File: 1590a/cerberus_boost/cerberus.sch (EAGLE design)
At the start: 30 parts, among them Q1 2N5088, Q2 2N5088, Q3 2N5087

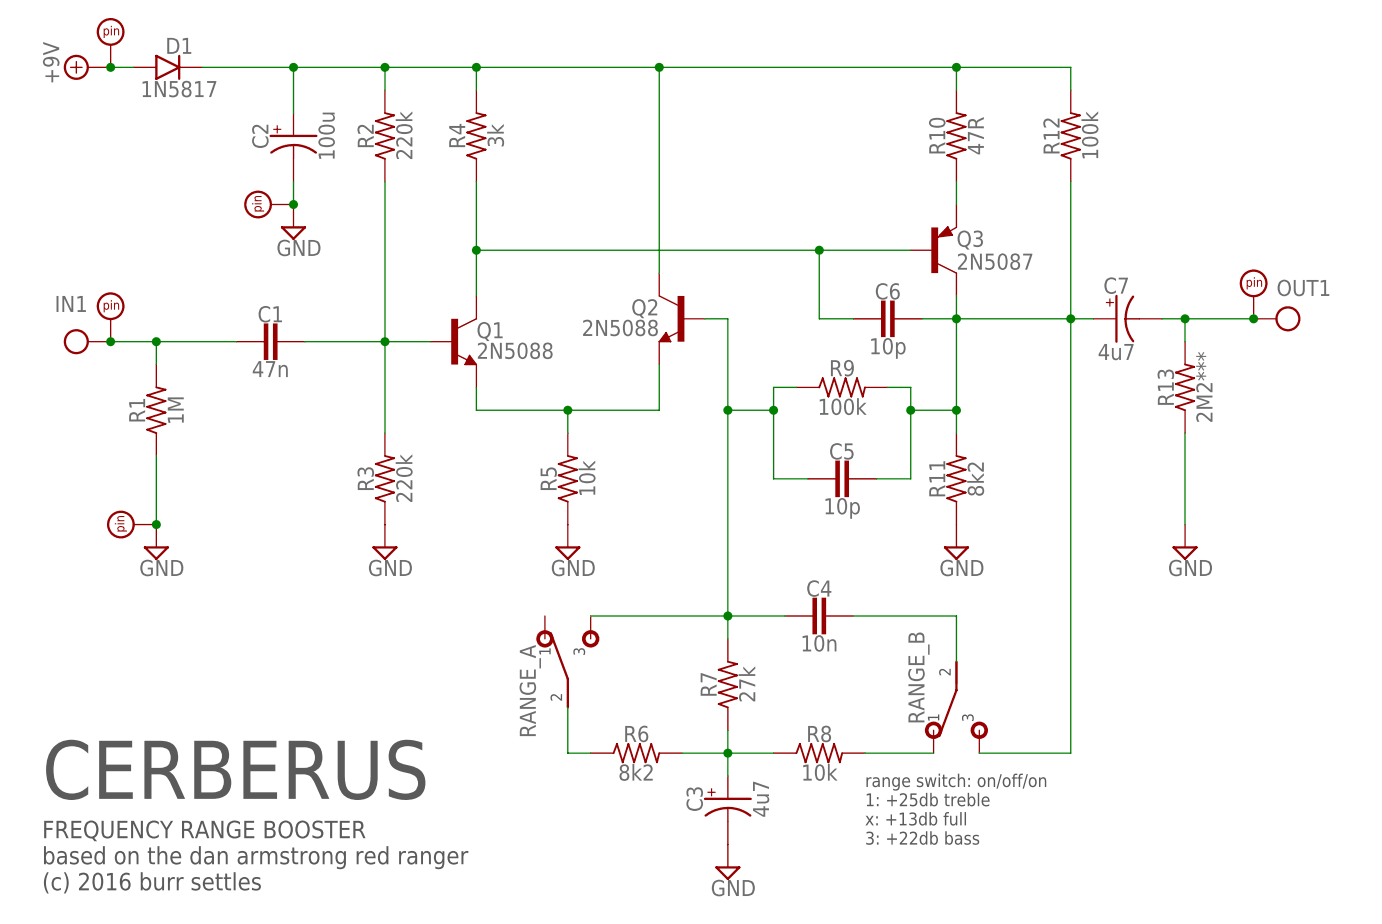
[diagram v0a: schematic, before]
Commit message: prettified schematics a bit
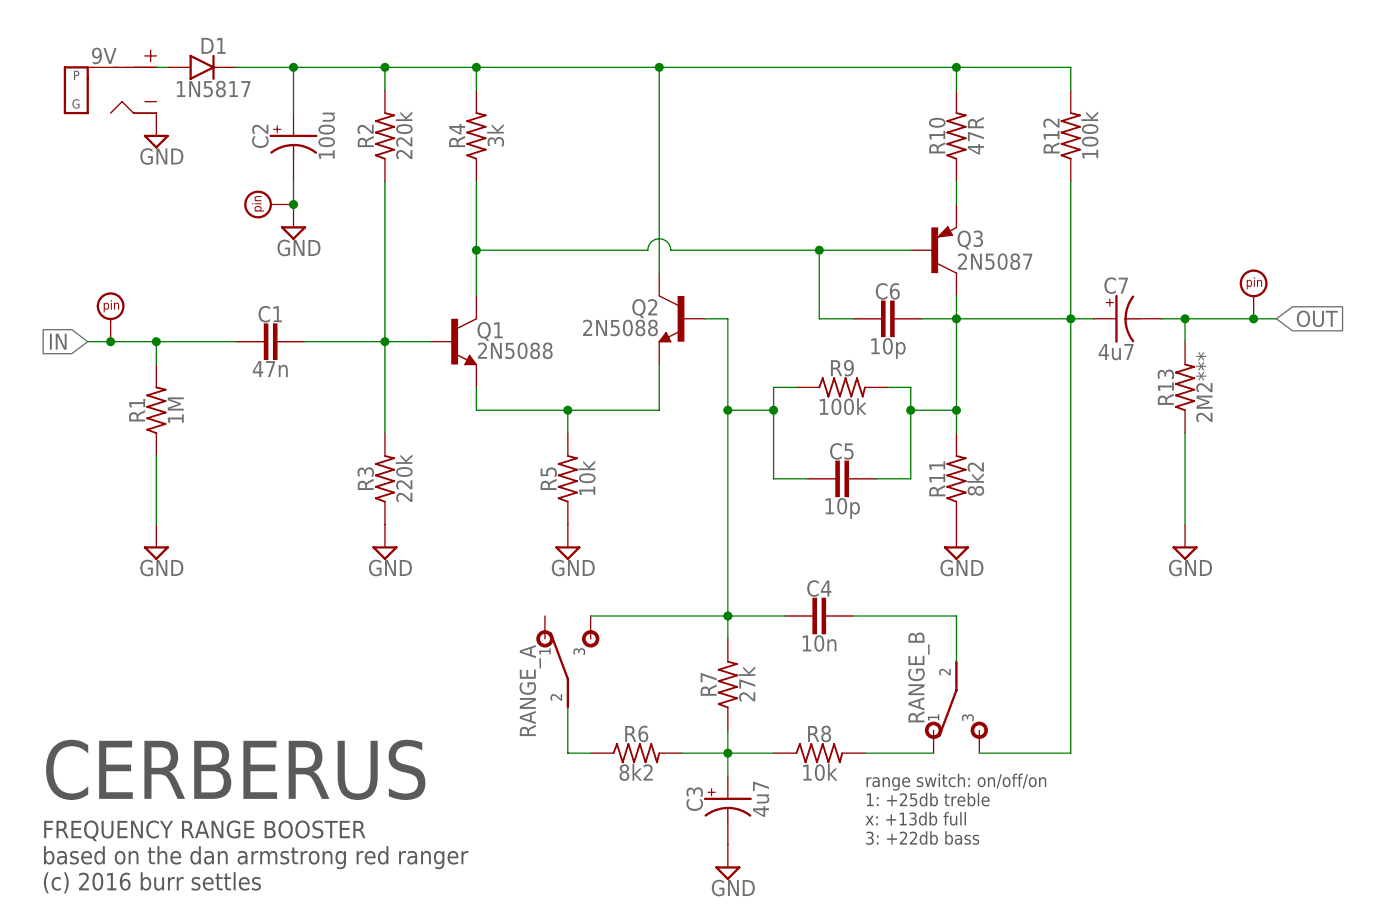
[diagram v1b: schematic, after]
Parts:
- removed PAD1: PADSQR, supply pins:PADSQR
- removed PAD3: PADRND, supply pins:PADRND
- added 9V: DC_MONO, jacks:DC_MONO
- D1: device diodes:DO41.2 -> diodes:DO41.3
- renumbered PAD2 to IN, PAD4 to GND, PAD5 to OUT
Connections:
- removed net +9V: D1.A, PAD1.P$1
- new net N$3: 9V.TIP, D1.A
- net GND: now also 9V.SLEEVE; no longer PAD3.P$1
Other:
- moved on the sheet: D1
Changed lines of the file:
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@@
 <drawing>
 <settings>
-<setting alwaysvectorfont="no"/>
+<setting alwaysvectorfont="yes"/>
 <setting verticaltext="up"/>
 </settings>
-<grid distance="0.1" unitdist="inch" unit="inch" style="lines" multiple="1" display="no" altdistance="0.01" altunitdist="inch" altunit="inch"/>
+<grid distance="0.05" unitdist="inch" unit="inch" style="lines" multiple="2" display="no" altdistance="0.01" altunitdist="inch" altunit="inch"/>
 <layers>
 <layer number="1" name="Top" color="4" fill="1" visible="no" active="no"/>
@@
 </classes>
 <parts>
-<part name="V1" library="gm-supply" deviceset="+9V" device=""/>
-<part name="IN1" library="gm-supply" deviceset="IN" device=""/>
-<part name="OUT1" library="gm-supply" deviceset="OUT" device=""/>
 <part name="C2" library="capacitors-elec" deviceset="050" device="1" value="100u"/>
 <part name="R2" library="resistors" deviceset="R_" device=".3B" value="220k"/>
@@
 <part name="GND5" library="gm-supply" deviceset="GND" device=""/>
 <part name="GND3" library="gm-supply" deviceset="GND" device=""/>
-<part name="PAD5" library="supply pins" deviceset="PAD" device="SQR"/>
-<part name="PAD2" library="supply pins" deviceset="PAD" device="SQR"/>
-<part name="PAD1" library="supply pins" deviceset="PAD" device="SQR"/>
-<part name="PAD3" library="supply pins" deviceset="PAD" device="RND"/>
-<part name="PAD4" library="supply pins" deviceset="PAD" device="RND"/>
+<part name="OUT" library="supply pins" deviceset="PAD" device="SQR"/>
+<part name="IN" library="supply pins" deviceset="PAD" device="SQR"/>
+<part name="GND" library="supply pins" deviceset="PAD" device="RND"/>
 <part name="R1" library="resistors" deviceset="R_" device=".3B" value="1M"/>
 <part name="GND1" library="gm-supply" deviceset="GND" device=""/>
@@
 <part name="R13" library="resistors" deviceset="R_" device=".3B" value="2M2***"/>
 <part name="GND7" library="gm-supply" deviceset="GND" device=""/>
-<part name="D1" library="diodes" deviceset="DO41" device=".2" value="1N5817"/>
+<part name="D1" library="diodes" deviceset="DO41" device=".3" value="1N5817"/>
+<part name="9V" library="jacks" deviceset="DC_MONO" device=""/>
+<part name="GND8" library="gm-supply" deviceset="GND" device=""/>
 </parts>
 <sheets>
@@
 </plain>
 <instances>
-<instance part="V1" gate="+9V" x="7.62" y="93.98" rot="R90"/>
-<instance part="IN1" gate="G$1" x="7.62" y="63.5"/>
-<instance part="OUT1" gate="G$1" x="139.7" y="66.04"/>
 <instance part="C2" gate="1" x="30.48" y="86.36" rot="MR270"/>
 <instance part="R2" gate="G$1" x="40.64" y="86.36" rot="R90"/>
@@
 <instance part="GND5" gate="GND" x="78.74" y="5.08"/>
 <instance part="GND3" gate="GND" x="40.64" y="40.64"/>
-<instance part="PAD5" gate="G$1" x="137.16" y="66.04"/>
-<instance part="PAD2" gate="G$1" x="10.16" y="63.5"/>
-<instance part="PAD1" gate="G$1" x="10.16" y="93.98"/>
-<instance part="PAD3" gate="G$1" x="15.24" y="43.18" rot="R90"/>
-<instance part="PAD4" gate="G$1" x="30.48" y="78.74" rot="R90"/>
+<instance part="OUT" gate="G$1" x="137.16" y="66.04"/>
+<instance part="IN" gate="G$1" x="10.16" y="63.5"/>
+<instance part="GND" gate="G$1" x="30.48" y="78.74" rot="R90"/>
 <instance part="R1" gate="G$1" x="15.24" y="55.88" rot="R90"/>
 <instance part="GND1" gate="GND" x="15.24" y="40.64"/>
@@
 <instance part="R13" gate="G$1" x="129.54" y="58.42" rot="R90"/>
 <instance part="GND7" gate="GND" x="129.54" y="40.64"/>
-<instance part="D1" gate="G$1" x="17.78" y="93.98"/>
+<instance part="D1" gate="G$1" x="21.59" y="93.98"/>
+<instance part="9V" gate="DC" x="10.16" y="91.44"/>
+<instance part="GND8" gate="GND" x="15.24" y="86.36"/>
 </instances>
 <busses>
 </busses>
 <nets>
-<net name="IN" class="0">
-<segment>
-<pinref part="IN1" gate="G$1" pin="IN"/>
-<pinref part="C1" gate="G$1" pin="2"/>
-<pinref part="PAD2" gate="G$1" pin="P$1"/>
-<wire x1="10.16" y1="63.5" x2="15.24" y2="63.5" width="0.1524" layer="91"/>
-<junction x="10.16" y="63.5"/>
-<pinref part="R1" gate="G$1" pin="2"/>
-<wire x1="15.24" y1="63.5" x2="24.13" y2="63.5" width="0.1524" layer="91"/>
-<wire x1="15.24" y1="60.96" x2="15.24" y2="63.5" width="0.1524" layer="91"/>
-<junction x="15.24" y="63.5"/>
-</segment>
-</net>
 <net name="N$1" class="0">
 <segment>
@@
 </segment>
 </net>
-<net name="+9V" class="0">
-<segment>
-<pinref part="D1" gate="G$1" pin="A"/>
-<wire x1="10.16" y1="93.98" x2="12.7" y2="93.98" width="0.1524" layer="91"/>
-<pinref part="PAD1" gate="G$1" pin="P$1"/>
-<junction x="10.16" y="93.98"/>
-<pinref part="V1" gate="+9V" pin="+9V"/>
-</segment>
-</net>
 <net name="N$2" class="0">
 <segment>
@@
 <wire x1="99.06" y1="73.66" x2="88.9" y2="73.66" width="0.1524" layer="91"/>
 <junction x="50.8" y="73.66"/>
-<wire x1="88.9" y1="73.66" x2="50.8" y2="73.66" width="0.1524" layer="91"/>
+<wire x1="88.9" y1="73.66" x2="72.39" y2="73.66" width="0.1524" layer="91"/>
+<wire x1="69.85" y1="73.66" x2="50.8" y2="73.66" width="0.1524" layer="91"/>
 <wire x1="92.71" y1="66.04" x2="88.9" y2="66.04" width="0.1524" layer="91"/>
 <wire x1="88.9" y1="66.04" x2="88.9" y2="73.66" width="0.1524" layer="91"/>
 <junction x="88.9" y="73.66"/>
 <pinref part="C6" gate="G$1" pin="2"/>
+<wire x1="69.85" y1="73.66" x2="72.39" y2="73.66" width="0.1524" layer="91" curve="-180" cap="flat"/>
 </segment>
 </net>
@@
 </segment>
 </net>
-<net name="OUT" class="0">
-<segment>
-<pinref part="OUT1" gate="G$1" pin="OUT"/>
-<pinref part="PAD5" gate="G$1" pin="P$1"/>
-<pinref part="C7" gate="1" pin="-"/>
-<wire x1="127" y1="66.04" x2="129.54" y2="66.04" width="0.1524" layer="91"/>
-<wire x1="129.54" y1="66.04" x2="137.16" y2="66.04" width="0.1524" layer="91"/>
-<pinref part="R13" gate="G$1" pin="2"/>
-<wire x1="129.54" y1="63.5" x2="129.54" y2="66.04" width="0.1524" layer="91"/>
-<junction x="129.54" y="66.04"/>
-<junction x="137.16" y="66.04"/>
-</segment>
-</net>
 <net name="N$10" class="0">
 <segment>
@@
 <pinref part="C2" gate="1" pin="-"/>
 <pinref part="GND2" gate="GND" pin="GND"/>
-<pinref part="PAD4" gate="G$1" pin="P$1"/>
+<pinref part="GND" gate="G$1" pin="P$1"/>
 <junction x="30.48" y="78.74"/>
 <wire x1="30.48" y1="78.74" x2="30.48" y2="81.28" width="0.1524" layer="91"/>
@@
 <wire x1="15.24" y1="50.8" x2="15.24" y2="43.18" width="0.1524" layer="91"/>
 <pinref part="GND1" gate="GND" pin="GND"/>
-<pinref part="PAD3" gate="G$1" pin="P$1"/>
-<junction x="15.24" y="43.18"/>
 </segment>
 <segment>
@@
 <wire x1="129.54" y1="53.34" x2="129.54" y2="43.18" width="0.1524" layer="91"/>
 </segment>
+<segment>
+<pinref part="9V" gate="DC" pin="SLEEVE"/>
+<pinref part="GND8" gate="GND" pin="GND"/>
+</segment>
 </net>
 <net name="N$7" class="0">
 <segment>
 <pinref part="R12" gate="G$1" pin="2"/>
-<wire x1="20.32" y1="93.98" x2="30.48" y2="93.98" width="0.1524" layer="91"/>
+<wire x1="24.13" y1="93.98" x2="30.48" y2="93.98" width="0.1524" layer="91"/>
 <wire x1="30.48" y1="93.98" x2="40.64" y2="93.98" width="0.1524" layer="91"/>
 <wire x1="40.64" y1="93.98" x2="50.8" y2="93.98" width="0.1524" layer="91"/>
@@
 </segment>
 </net>
+<net name="N$3" class="0">
+<segment>
+<pinref part="D1" gate="G$1" pin="A"/>
+<wire x1="15.24" y1="93.98" x2="16.51" y2="93.98" width="0.1524" layer="91"/>
+<pinref part="9V" gate="DC" pin="TIP"/>
+</segment>
+</net>
+<net name="IN" class="0">
+<segment>
+<pinref part="C1" gate="G$1" pin="2"/>
+<pinref part="IN" gate="G$1" pin="P$1"/>
+<wire x1="10.16" y1="63.5" x2="15.24" y2="63.5" width="0.1524" layer="91"/>
+<pinref part="R1" gate="G$1" pin="2"/>
+<wire x1="15.24" y1="63.5" x2="24.13" y2="63.5" width="0.1524" layer="91"/>
+<wire x1="15.24" y1="60.96" x2="15.24" y2="63.5" width="0.1524" layer="91"/>
+<junction x="15.24" y="63.5"/>
+<label x="7.62" y="63.5" size="1.778" layer="95" rot="R180" xref="yes"/>
+<wire x1="7.62" y1="63.5" x2="10.16" y2="63.5" width="0.1524" layer="91"/>
+<junction x="10.16" y="63.5"/>
+</segment>
+</net>
+<net name="OUT" class="0">
+<segment>
+<pinref part="OUT" gate="G$1" pin="P$1"/>
+<pinref part="C7" gate="1" pin="-"/>
+<wire x1="127" y1="66.04" x2="129.54" y2="66.04" width="0.1524" layer="91"/>
+<wire x1="129.54" y1="66.04" x2="137.16" y2="66.04" width="0.1524" layer="91"/>
+<pinref part="R13" gate="G$1" pin="2"/>
+<wire x1="129.54" y1="63.5" x2="129.54" y2="66.04" width="0.1524" layer="91"/>
+<junction x="129.54" y="66.04"/>
+<label x="139.7" y="66.04" size="1.778" layer="95" xref="yes"/>
+<wire x1="139.7" y1="66.04" x2="137.16" y2="66.04" width="0.1524" layer="91"/>
+<junction x="137.16" y="66.04"/>
+</segment>
+</net>

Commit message: added RT logo; converted some pots trimmers
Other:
- note added: "FREQUENCY RANGE BOOSTER based on the dan armstrong red ranger (c)2016 burr settles"
- note removed: "FREQUENCY RANGE BOOSTER based on the dan armstrong red ranger (c) 2016 burr settles"
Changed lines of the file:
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@@
 <setting verticaltext="up"/>
 </settings>
-<grid distance="0.05" unitdist="inch" unit="inch" style="lines" multiple="2" display="no" altdistance="0.01" altunitdist="inch" altunit="inch"/>
+<grid distance="0.1" unitdist="inch" unit="inch" style="lines" multiple="1" display="no" altdistance="0.01" altunitdist="inch" altunit="inch"/>
 <layers>
 <layer number="1" name="Top" color="4" fill="1" visible="no" active="no"/>
@@
 <part name="9V" library="jacks" deviceset="DC_MONO" device=""/>
 <part name="GND8" library="gm-supply" deviceset="GND" device=""/>
+<part name="U$2" library="logos" deviceset="REBELSTRUST" device=""/>
 </parts>
 <sheets>
@@
 <text x="2.54" y="2.54" size="1.9304" layer="97">FREQUENCY RANGE BOOSTER
 based on the dan armstrong red ranger
-(c) 2016 burr settles</text>
+(c)2016 burr settles</text>
 <text x="93.98" y="7.62" size="1.4224" layer="97">range switch: on/off/on
 1: +25db treble
@@
 <instance part="9V" gate="DC" x="10.16" y="91.44"/>
 <instance part="GND8" gate="GND" x="15.24" y="86.36"/>
+<instance part="U$2" gate="G$1" x="2.54" y="22.86"/>
 </instances>
 <busses>

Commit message: updates to cerberus and cyclops
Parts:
- R13: value 2M2*** -> 1M
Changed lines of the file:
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@@
 <part name="GND6" library="gm-supply" deviceset="GND" device=""/>
 <part name="GND4" library="gm-supply" deviceset="GND" device=""/>
-<part name="R13" library="resistors" deviceset="R_" device=".3B" value="2M2***"/>
+<part name="R13" library="resistors" deviceset="R_" device=".3B" value="1M"/>
 <part name="GND7" library="gm-supply" deviceset="GND" device=""/>
 <part name="D1" library="diodes" deviceset="DO41" device=".3" value="1N5817"/>

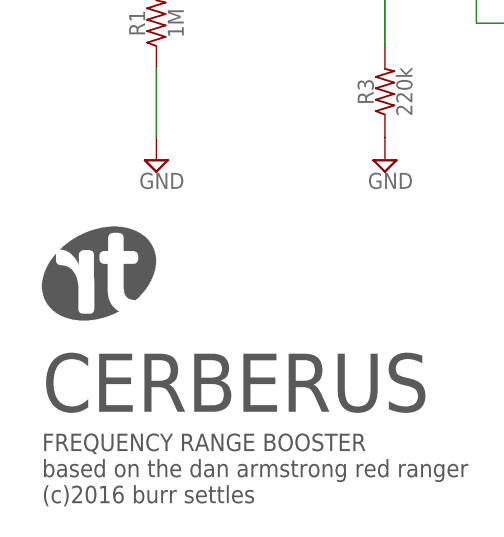
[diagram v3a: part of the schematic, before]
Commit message: convert bitmap logos to polygons
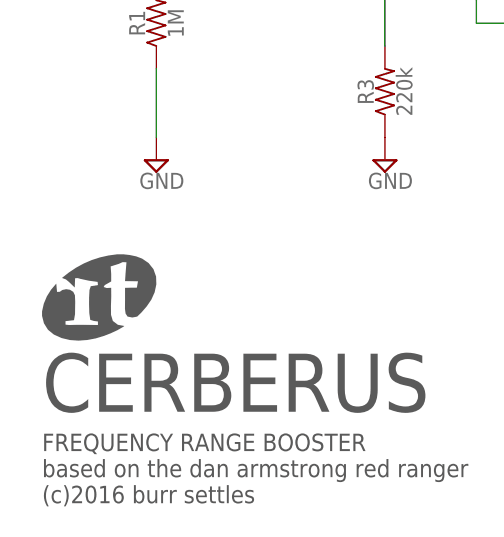
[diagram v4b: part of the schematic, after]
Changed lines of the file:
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@@
 <instance part="9V" gate="DC" x="10.16" y="91.44"/>
 <instance part="GND8" gate="GND" x="15.24" y="86.36"/>
-<instance part="U$2" gate="G$1" x="2.54" y="22.86"/>
+<instance part="U$2" gate="G$1" x="2.54" y="20.32"/>
 </instances>
 <busses>

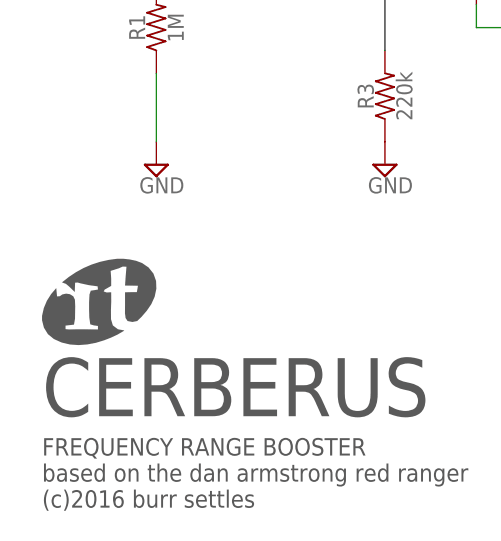
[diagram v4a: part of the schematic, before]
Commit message: updated library + logos
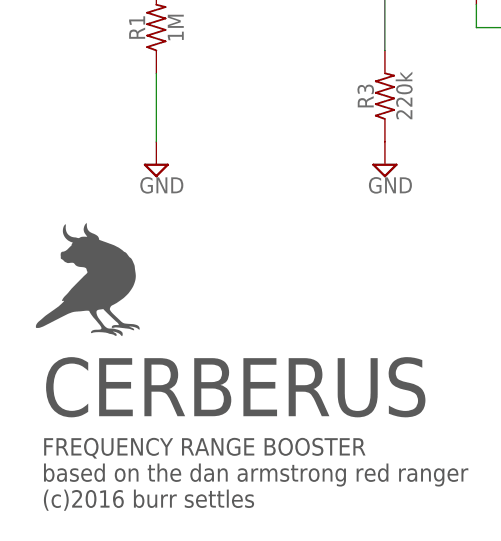
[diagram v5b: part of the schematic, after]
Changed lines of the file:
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@@
 <part name="9V" library="jacks" deviceset="DC_MONO" device=""/>
 <part name="GND8" library="gm-supply" deviceset="GND" device=""/>
-<part name="U$2" library="logos" deviceset="REBELSTRUST" device=""/>
+<part name="BF1" library="logos" deviceset="BULLFINCH" device=""/>
 </parts>
 <sheets>
@@
 <instance part="9V" gate="DC" x="10.16" y="91.44"/>
 <instance part="GND8" gate="GND" x="15.24" y="86.36"/>
-<instance part="U$2" gate="G$1" x="2.54" y="20.32"/>
+<instance part="BF1" gate="G$1" x="7.62" y="27.94"/>
 </instances>
 <busses>
